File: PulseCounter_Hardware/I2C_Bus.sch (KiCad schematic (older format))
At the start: 32 parts, among them U1 74LV8154, U10 74LV8154, U11 74LV8154, U12 74LV8154, U13 74LV8154, U14 MCP23008-E_P, U15 MCP23008-E_P, U16 MCP23008-E_P, U17 MCP23008-E_P, U18 74LV8154, U19 74LV8154, U2 74LV8154, U20 74LV8154, U21 74LV8154, U22 MCP23008-E_P, U23 MCP23008-E_P, U24 MCP23008-E_P, U25 MCP23008-E_P, U26 74LV8154, U27 74LV8154, U28 74LV8154, U29 74LV8154, U3 74LV8154, U30 MCP23008-E_P, U31 MCP23008-E_P, U32 MCP23008-E_P, U33 MCP23008-E_P, U4 74LV8154, U6 MCP23008-E_P, U7 MCP23008-E_P, U8 MCP23008-E_P, U9 MCP23008-E_P

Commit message: Starting with MCU
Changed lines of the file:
@@
 	5650 5200 4900 5200
 Wire Wire Line
-	2650 5200 1900 5200
-Wire Wire Line
 	1900 5300 2650 5300
 Wire Wire Line
@@
 Wire Wire Line
 	2650 5600 1900 5600
-Wire Wire Line
-	1900 5700 2650 5700
 Wire Wire Line
 	2650 5800 1900 5800
@@
 Text Label 3050 5000 0    50   ~ 0
 3V3
-$Comp
-L dk_Interface-I-O-Expanders:MCP23008-E_P U?
-U 1 1 5F726361
-P 3150 5700
-AR Path="/5F726361" Ref="U?"  Part="1"
-AR Path="/5F71652A/5F726361" Ref="U8"  Part="1"
-F 0 "U8" H 2850 6450 60  0000 C CNN
-F 1 "MCP23008-E_P" H 3150 6550 60  0000 C CNN
-F 2 "digikey-footprints:DIP-18_W7.62mm" H 3350 5900 60  0001 L CNN
-F 3 "http://www.microchip.com/mymicrochip/filehandler.aspx?ddocname=en021920" H 3350 6000 60  0001 L CNN
-F 4 "MCP23008-E/P-ND" H 3350 6100 60  0001 L CNN "Digi-Key_PN"
-F 5 "MCP23008-E/P" H 3350 6200 60  0001 L CNN "MPN"
-F 6 "Integrated Circuits (ICs)" H 3350 6300 60  0001 L CNN "Category"
-F 7 "Interface - I/O Expanders" H 3350 6400 60  0001 L CNN "Family"
-F 8 "http://www.microchip.com/mymicrochip/filehandler.aspx?ddocname=en021920" H 3350 6500 60  0001 L CNN "DK_Datasheet_Link"
-F 9 "/product-detail/en/microchip-technology/MCP23008-E-P/MCP23008-E-P-ND/735951" H 3350 6600 60  0001 L CNN "DK_Detail_Page"
-F 10 "IC I/O EXPANDER I2C 8B 18DIP" H 3350 6700 60  0001 L CNN "Description"
-F 11 "Microchip Technology" H 3350 6800 60  0001 L CNN "Manufacturer"
-F 12 "Active" H 3350 6900 60  0001 L CNN "Status"
-	1    3150 5700
-	1    0    0    -1
-$EndComp
 $Comp
 L 74xx:74LV8154 U?
@@
 F32 "CHANNEL_OUT_30" O L 14550 6200 50
 F33 "CHANNEL_OUT_31" O L 14550 6300 50
+F34 "GND" U R 15650 6350 50
+F35 "3V3" U R 15650 6200 50
 $EndSheet
+Text Label 14050 6200 2    50   ~ 0
+CHANNEL_IN_30
+Text Label 14050 6300 2    50   ~ 0
+CHANNEL_IN_31
+Text Label 14050 6100 2    50   ~ 0
+CHANNEL_IN_29
+Text Label 14050 6000 2    50   ~ 0
+CHANNEL_IN_28
+Text Label 14050 5900 2    50   ~ 0
+CHANNEL_IN_27
+Text Label 14050 5800 2    50   ~ 0
+CHANNEL_IN_26
+Text Label 14050 5600 2    50   ~ 0
+CHANNEL_IN_24
+Text Label 14050 5700 2    50   ~ 0
+CHANNEL_IN_25
+Text Label 14050 5200 2    50   ~ 0
+CHANNEL_IN_20
+Text Label 14050 5500 2    50   ~ 0
+CHANNEL_IN_23
+Text Label 14050 5400 2    50   ~ 0
+CHANNEL_IN_22
+Text Label 14050 5300 2    50   ~ 0
+CHANNEL_IN_21
+Text Label 14050 5000 2    50   ~ 0
+CHANNEL_IN_18
+Text Label 14050 5100 2    50   ~ 0
+CHANNEL_IN_19
+Text Label 14050 4900 2    50   ~ 0
+CHANNEL_IN_17
+Text Label 14050 4800 2    50   ~ 0
+CHANNEL_IN_16
+Text Label 14050 4700 2    50   ~ 0
+CHANNEL_IN_15
+Text Label 14050 4600 2    50   ~ 0
+CHANNEL_IN_14
+Text Label 14050 4400 2    50   ~ 0
+CHANNEL_IN_12
+Text Label 14050 4500 2    50   ~ 0
+CHANNEL_IN_13
+Text Label 14050 4300 2    50   ~ 0
+CHANNEL_IN_11
+Text Label 14050 4200 2    50   ~ 0
+CHANNEL_IN_10
+Text Label 14050 4100 2    50   ~ 0
+CHANNEL_IN_9
+Text Label 14050 4000 2    50   ~ 0
+CHANNEL_IN_8
+Text Label 14050 3800 2    50   ~ 0
+CHANNEL_IN_6
+Text Label 14050 3900 2    50   ~ 0
+CHANNEL_IN_7
+Text Label 14050 3700 2    50   ~ 0
+CHANNEL_IN_5
+Text Label 14050 3600 2    50   ~ 0
+CHANNEL_IN_4
+Text Label 14050 3500 2    50   ~ 0
+CHANNEL_IN_3
+Text Label 14050 3400 2    50   ~ 0
+CHANNEL_IN_2
+Text Label 14050 3200 2    50   ~ 0
+CHANNEL_IN_0
+Text Label 14050 3300 2    50   ~ 0
+CHANNEL_IN_1
+Wire Wire Line
+	14050 3200 14550 3200
+Wire Wire Line
+	14550 3300 14050 3300
+Wire Wire Line
+	14050 3400 14550 3400
+Wire Wire Line
+	14050 3500 14550 3500
+Wire Wire Line
+	14550 3600 14050 3600
+Wire Wire Line
+	14050 3700 14550 3700
+Wire Wire Line
+	14050 3800 14550 3800
+Wire Wire Line
+	14550 3900 14050 3900
+Wire Wire Line
+	14050 4000 14550 4000
+Wire Wire Line
+	14050 4100 14550 4100
+Wire Wire Line
+	14550 4200 14050 4200
+Wire Wire Line
+	14050 4300 14550 4300
+Wire Wire Line
+	14050 4400 14550 4400
+Wire Wire Line
+	14550 4500 14050 4500
+Wire Wire Line
+	14050 4600 14550 4600
+Wire Wire Line
+	14050 4700 14550 4700
+Wire Wire Line
+	14550 4800 14050 4800
+Wire Wire Line
+	14050 4900 14550 4900
+Wire Wire Line
+	14050 5000 14550 5000
+Wire Wire Line
+	14550 5100 14050 5100
+Wire Wire Line
+	14050 5200 14550 5200
+Wire Wire Line
+	14050 5300 14550 5300
+Wire Wire Line
+	14550 5400 14050 5400
+Wire Wire Line
+	14050 5500 14550 5500
+Wire Wire Line
+	14050 5600 14550 5600
+Wire Wire Line
+	14550 5700 14050 5700
+Wire Wire Line
+	14050 5800 14550 5800
+Wire Wire Line
+	14050 5900 14550 5900
+Wire Wire Line
+	14550 6000 14050 6000
+Wire Wire Line
+	14050 6100 14550 6100
+Wire Wire Line
+	14050 6200 14550 6200
+Wire Wire Line
+	14550 6300 14050 6300
+Wire Wire Line
+	1900 5700 2650 5700
+Wire Wire Line
+	2650 5200 1900 5200
+$Comp
+L dk_Interface-I-O-Expanders:MCP23008-E_P U?
+U 1 1 5F726361
+P 3150 5700
+AR Path="/5F726361" Ref="U?"  Part="1"
+AR Path="/5F71652A/5F726361" Ref="U8"  Part="1"
+F 0 "U8" H 2850 6450 60  0000 C CNN
+F 1 "MCP23008-E_P" H 3150 6550 60  0000 C CNN
+F 2 "digikey-footprints:DIP-18_W7.62mm" H 3350 5900 60  0001 L CNN
+F 3 "http://www.microchip.com/mymicrochip/filehandler.aspx?ddocname=en021920" H 3350 6000 60  0001 L CNN
+F 4 "MCP23008-E/P-ND" H 3350 6100 60  0001 L CNN "Digi-Key_PN"
+F 5 "MCP23008-E/P" H 3350 6200 60  0001 L CNN "MPN"
+F 6 "Integrated Circuits (ICs)" H 3350 6300 60  0001 L CNN "Category"
+F 7 "Interface - I/O Expanders" H 3350 6400 60  0001 L CNN "Family"
+F 8 "http://www.microchip.com/mymicrochip/filehandler.aspx?ddocname=en021920" H 3350 6500 60  0001 L CNN "DK_Datasheet_Link"
+F 9 "/product-detail/en/microchip-technology/MCP23008-E-P/MCP23008-E-P-ND/735951" H 3350 6600 60  0001 L CNN "DK_Detail_Page"
+F 10 "IC I/O EXPANDER I2C 8B 18DIP" H 3350 6700 60  0001 L CNN "Description"
+F 11 "Microchip Technology" H 3350 6800 60  0001 L CNN "Manufacturer"
+F 12 "Active" H 3350 6900 60  0001 L CNN "Status"
+	1    3150 5700
+	1    0    0    -1
+$EndComp
+Text Label 15650 6200 0    50   ~ 0
+3V3
+Text Label 15650 6350 0    50   ~ 0
+GND
 $EndSCHEMATC

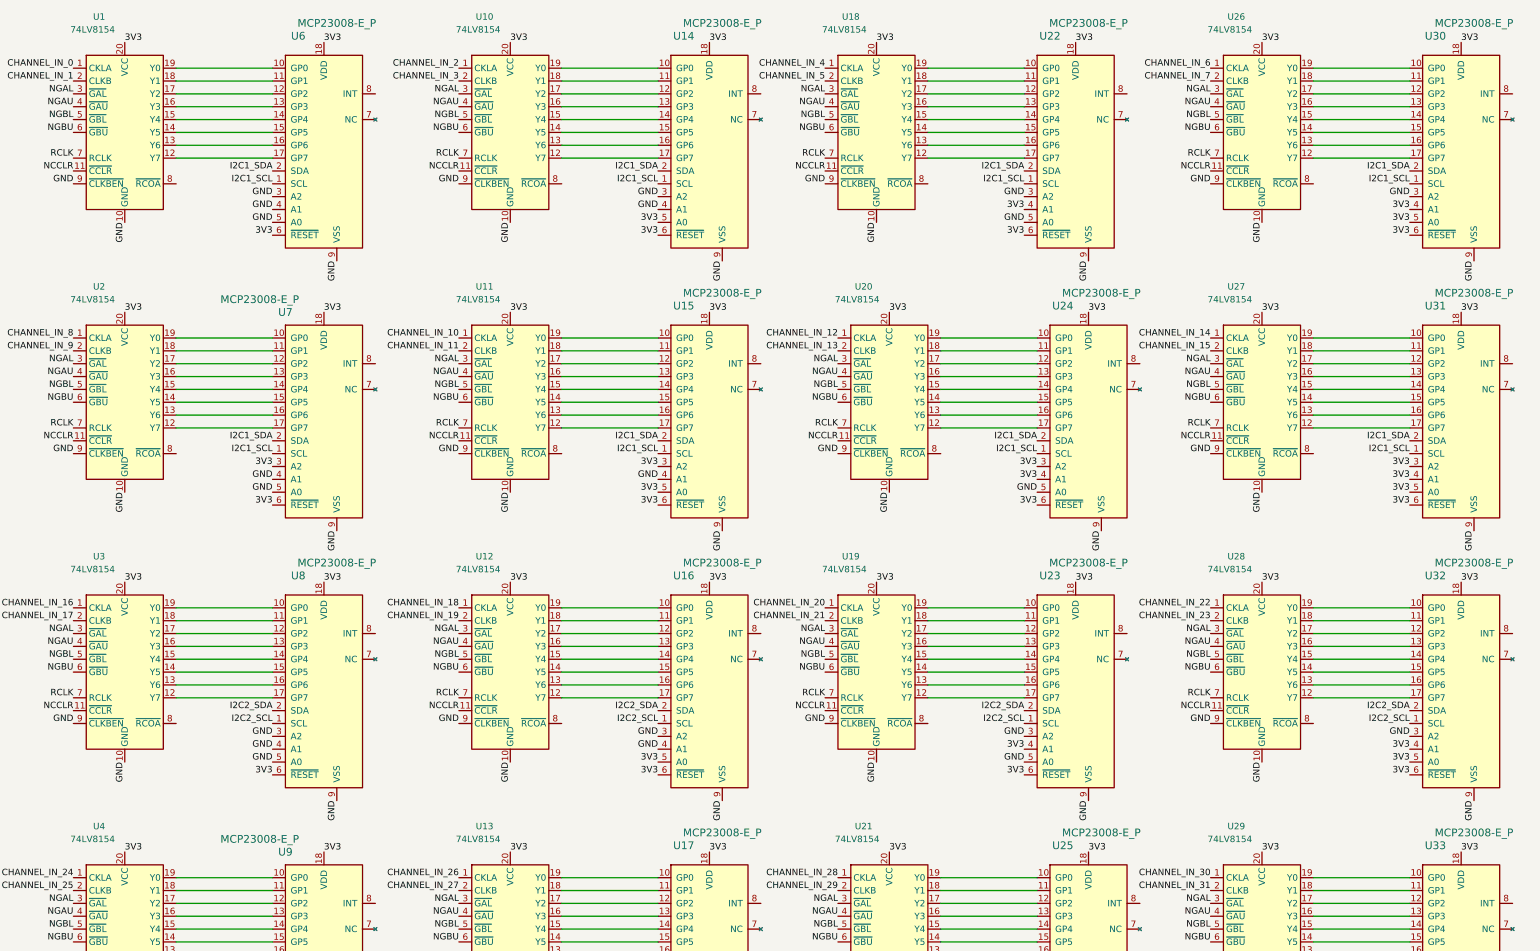
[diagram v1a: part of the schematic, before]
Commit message: Added SPI flash, connected I2C, SPI
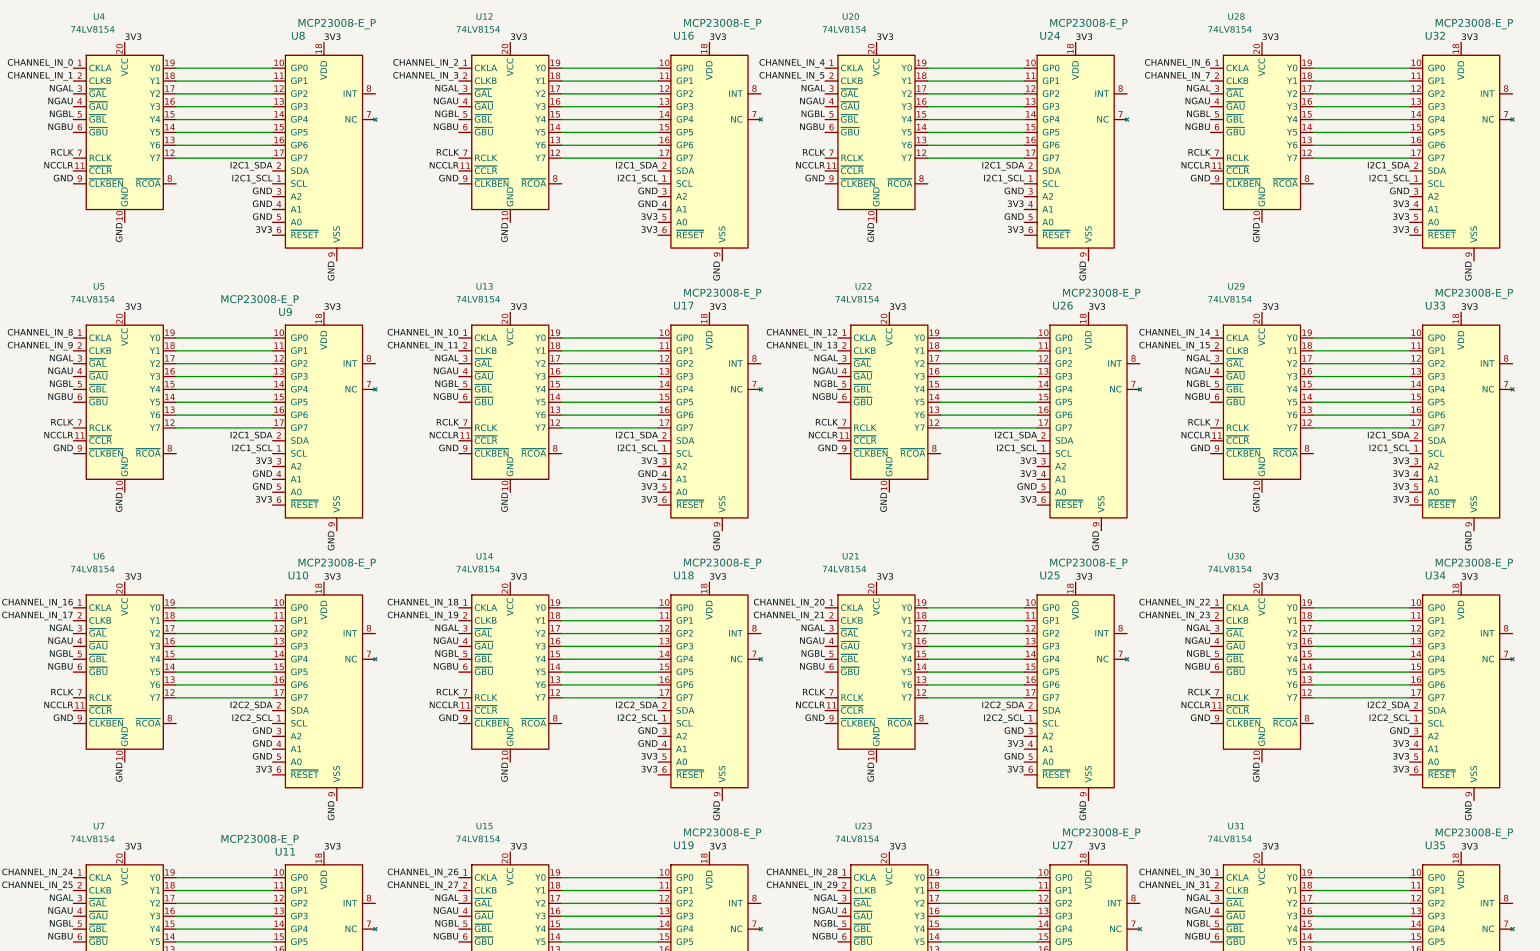
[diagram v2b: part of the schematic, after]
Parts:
- renumbered U8 to U10, U9 to U11, U10 to U12, U11 to U13, U12 to U14, U13 to U15, U14 to U16, U15 to U17, U16 to U18, U17 to U19, U18 to U20, U19 to U21, U20 to U22, U21 to U23, U22 to U24, U23 to U25, U24 to U26, U25 to U27, U26 to U28, U27 to U29, U28 to U30, U29 to U31, U30 to U32, U31 to U33, U32 to U34, U33 to U35, U1 to U4, U2 to U5, U3 to U6, U4 to U7, U6 to U8, U7 to U9

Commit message: Added correct varistor
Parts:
- U10, U11, U16, U17, U18, U19, U24, U25, U26, U27, U32, U33, U34, U35, U8, U9: footprint digikey-footprints:DIP-18_W7.62mm -> digikey-footprints:SOIC-18_W7.5mm
- U12, U13, U14, U15, U20, U21, U22, U23, U28, U29, U30, U31, U4, U5, U6, U7: footprint (none) -> Package_SO:TSSOP-20_4.4x6.5mm_P0.65mm
